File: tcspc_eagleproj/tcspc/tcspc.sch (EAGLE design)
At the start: 0 parts

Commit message: Added the THS788 to the sch, made a simple brd with the 788 on it. Created a gitattributes file so I don't keep getting crlf messages for eagle files.
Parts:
- added U1: THS788, tcspc_lib:THS788
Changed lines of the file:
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@@
 <parts>
 <part name="FRAME1" library="frames" library_urn="urn:adsk.eagle:library:229" deviceset="FRAME_A_L" device=""/>
+<part name="U1" library="tcspc_lib" deviceset="THS788" device=""/>
 </parts>
 <sheets>
@@
 <instance part="FRAME1" gate="G$1" x="0" y="0"/>
 <instance part="FRAME1" gate="G$2" x="172.72" y="0"/>
+<instance part="U1" gate="G$1" x="129.54" y="99.06"/>
 </instances>
 <busses>
+</busses>
+<nets>
+</nets>
+</sheet>
+<sheet>
+<plain>
+</plain>
+<instances>
+</instances>
+<busses>

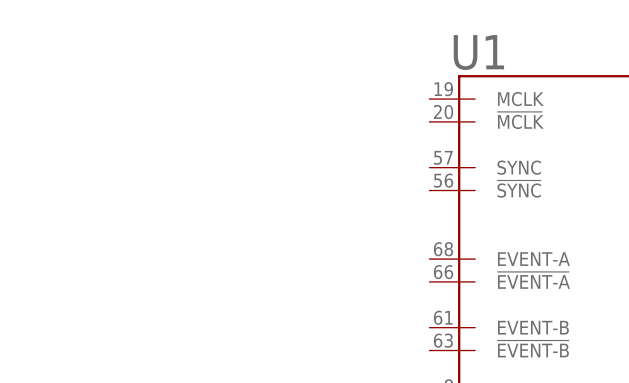
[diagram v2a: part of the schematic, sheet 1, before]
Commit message: added the SiT5021 Oscillator to the library
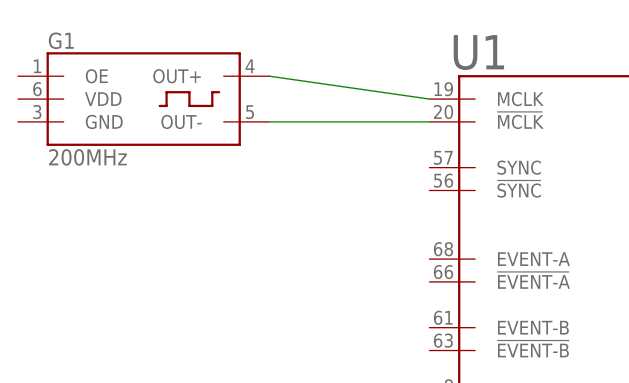
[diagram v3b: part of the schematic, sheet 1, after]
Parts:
- added G1: 200MHz, tcspc_lib:SIT5021
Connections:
- new net N$1: G1.OUT-, U1.!MCLK
- new net N$2: G1.OUT+, U1.MCLK
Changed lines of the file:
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@@
 <part name="FRAME1" library="frames" library_urn="urn:adsk.eagle:library:229" deviceset="FRAME_A_L" device=""/>
 <part name="U1" library="tcspc_lib" deviceset="THS788" device=""/>
+<part name="G1" library="tcspc_lib" deviceset="SIT5021" device="" value="200MHz"/>
 </parts>
 <sheets>
@@
 <instance part="FRAME1" gate="G$2" x="172.72" y="0"/>
 <instance part="U1" gate="G$1" x="129.54" y="99.06"/>
+<instance part="G1" gate="G$1" x="76.2" y="139.7"/>
 </instances>
 <busses>
 </busses>
 <nets>
+<net name="N$1" class="0">
+<segment>
+<pinref part="G1" gate="G$1" pin="OUT-"/>
+<pinref part="U1" gate="G$1" pin="!MCLK"/>
+<wire x1="91.44" y1="137.16" x2="109.22" y2="137.16" width="0.1524" layer="91"/>
+</segment>
+</net>
+<net name="N$2" class="0">
+<segment>
+<pinref part="U1" gate="G$1" pin="MCLK"/>
+<pinref part="G1" gate="G$1" pin="OUT+"/>
+<wire x1="109.22" y1="139.7" x2="91.44" y2="142.24" width="0.1524" layer="91"/>
+</segment>
+</net>
 </nets>
 </sheet>

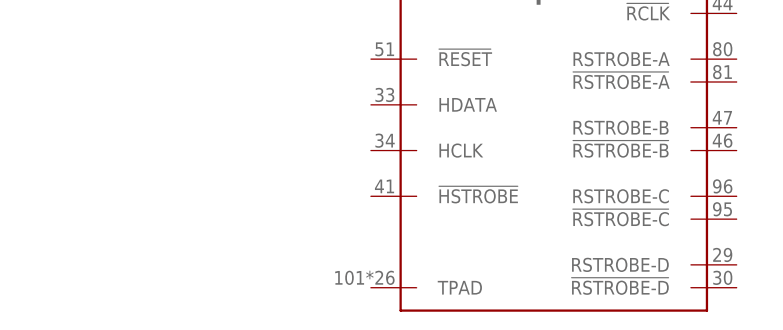
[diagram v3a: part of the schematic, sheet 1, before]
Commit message: threw a couple SMAs and DACs onto the schematic
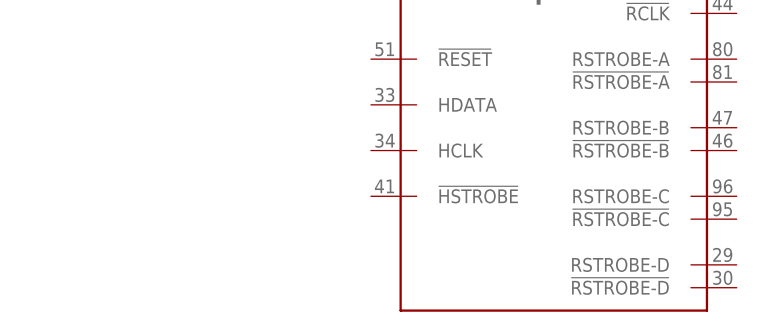
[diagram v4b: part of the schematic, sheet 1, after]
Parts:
- added U2, U3, U4, U5: MCP4725, tcspc_lib:MCP4725
- added X1, X2, X3, X4: SMA, tcspc_lib:SMA
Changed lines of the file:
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@@
 <layer number="48" name="Document" color="7" fill="1" visible="no" active="no"/>
 <layer number="49" name="Reference" color="7" fill="1" visible="no" active="no"/>
+<layer number="50" name="dxf" color="7" fill="1" visible="no" active="no"/>
 <layer number="51" name="tDocu" color="7" fill="1" visible="no" active="no"/>
 <layer number="52" name="bDocu" color="7" fill="1" visible="no" active="no"/>
+<layer number="53" name="tGND_GNDA" color="7" fill="9" visible="no" active="no"/>
+<layer number="54" name="bGND_GNDA" color="1" fill="9" visible="no" active="no"/>
+<layer number="56" name="wert" color="7" fill="1" visible="no" active="no"/>
+<layer number="57" name="tCAD" color="7" fill="1" visible="no" active="no"/>
+<layer number="59" name="tCarbon" color="7" fill="1" visible="no" active="no"/>
+<layer number="60" name="bCarbon" color="7" fill="1" visible="no" active="no"/>
 <layer number="88" name="SimResults" color="9" fill="1" visible="yes" active="yes"/>
 <layer number="89" name="SimProbes" color="9" fill="1" visible="yes" active="yes"/>
@@
 <layer number="97" name="Info" color="7" fill="1" visible="yes" active="yes"/>
 <layer number="98" name="Guide" color="6" fill="1" visible="yes" active="yes"/>
+<layer number="99" name="SpiceOrder" color="7" fill="1" visible="yes" active="yes"/>
+<layer number="100" name="Muster" color="7" fill="1" visible="no" active="no"/>
+<layer number="101" name="Patch_Top" color="12" fill="4" visible="yes" active="yes"/>
+<layer number="102" name="Vscore" color="7" fill="1" visible="yes" active="yes"/>
+<layer number="103" name="tMap" color="7" fill="1" visible="yes" active="yes"/>
+<layer number="104" name="Name" color="16" fill="1" visible="yes" active="yes"/>
+<layer number="105" name="tPlate" color="7" fill="1" visible="yes" active="yes"/>
+<layer number="106" name="bPlate" color="7" fill="1" visible="yes" active="yes"/>
+<layer number="107" name="Crop" color="7" fill="1" visible="yes" active="yes"/>
+<layer number="108" name="tplace-old" color="10" fill="1" visible="yes" active="yes"/>
+<layer number="109" name="ref-old" color="11" fill="1" visible="yes" active="yes"/>
+<layer number="110" name="fp0" color="7" fill="1" visible="yes" active="yes"/>
+<layer number="111" name="LPC17xx" color="7" fill="1" visible="yes" active="yes"/>
+<layer number="112" name="tSilk" color="7" fill="1" visible="yes" active="yes"/>
+<layer number="113" name="IDFDebug" color="7" fill="1" visible="yes" active="yes"/>
+<layer number="114" name="Badge_Outline" color="7" fill="1" visible="yes" active="yes"/>
+<layer number="115" name="ReferenceISLANDS" color="7" fill="1" visible="yes" active="yes"/>
+<layer number="116" name="Patch_BOT" color="9" fill="4" visible="yes" active="yes"/>
+<layer number="118" name="Rect_Pads" color="7" fill="1" visible="yes" active="yes"/>
+<layer number="121" name="_tsilk" color="7" fill="1" visible="yes" active="yes"/>
+<layer number="122" name="_bsilk" color="7" fill="1" visible="yes" active="yes"/>
+<layer number="123" name="tTestmark" color="7" fill="1" visible="yes" active="yes"/>
+<layer number="124" name="bTestmark" color="7" fill="1" visible="yes" active="yes"/>
+<layer number="125" name="_tNames" color="7" fill="1" visible="yes" active="yes"/>
+<layer number="126" name="_bNames" color="7" fill="1" visible="yes" active="yes"/>
+<layer number="127" name="_tValues" color="7" fill="1" visible="yes" active="yes"/>
+<layer number="128" name="_bValues" color="7" fill="1" visible="yes" active="yes"/>
+<layer number="129" name="Mask" color="7" fill="1" visible="yes" active="yes"/>
+<layer number="131" name="tAdjust" color="7" fill="1" visible="yes" active="yes"/>
+<layer number="132" name="bAdjust" color="7" fill="1" visible="yes" active="yes"/>
+<layer number="144" name="Drill_legend" color="7" fill="1" visible="yes" active="yes"/>
+<layer number="150" name="Notes" color="7" fill="1" visible="yes" active="yes"/>
+<layer number="151" name="HeatSink" color="7" fill="1" visible="yes" active="yes"/>
+<layer number="152" name="_bDocu" color="7" fill="1" visible="yes" active="yes"/>
+<layer number="153" name="FabDoc1" color="7" fill="1" visible="yes" active="yes"/>
+<layer number="154" name="FabDoc2" color="7" fill="1" visible="yes" active="yes"/>
+<layer number="155" name="FabDoc3" color="7" fill="1" visible="yes" active="yes"/>
+<layer number="199" name="Contour" color="7" fill="1" visible="yes" active="yes"/>
+<layer number="200" name="200bmp" color="1" fill="10" visible="yes" active="yes"/>
+<layer number="201" name="201bmp" color="2" fill="10" visible="yes" active="yes"/>
+<layer number="202" name="202bmp" color="3" fill="10" visible="yes" active="yes"/>
+<layer number="203" name="203bmp" color="4" fill="10" visible="yes" active="yes"/>
+<layer number="204" name="204bmp" color="5" fill="10" visible="yes" active="yes"/>
+<layer number="205" name="205bmp" color="6" fill="10" visible="yes" active="yes"/>
+<layer number="206" name="206bmp" color="7" fill="10" visible="yes" active="yes"/>
+<layer number="207" name="207bmp" color="8" fill="10" visible="yes" active="yes"/>
+<layer number="208" name="208bmp" color="9" fill="10" visible="yes" active="yes"/>
+<layer number="209" name="209bmp" color="7" fill="1" visible="yes" active="yes"/>
+<layer number="210" name="210bmp" color="7" fill="1" visible="yes" active="yes"/>
+<layer number="211" name="211bmp" color="7" fill="1" visible="yes" active="yes"/>
+<layer number="212" name="212bmp" color="7" fill="1" visible="yes" active="yes"/>
+<layer number="213" name="213bmp" color="7" fill="1" visible="yes" active="yes"/>
+<layer number="214" name="214bmp" color="7" fill="1" visible="yes" active="yes"/>
+<layer number="215" name="215bmp" color="7" fill="1" visible="yes" active="yes"/>
+<layer number="216" name="216bmp" color="7" fill="1" visible="yes" active="yes"/>
+<layer number="217" name="217bmp" color="18" fill="1" visible="no" active="no"/>
+<layer number="218" name="218bmp" color="19" fill="1" visible="no" active="no"/>
+<layer number="219" name="219bmp" color="20" fill="1" visible="no" active="no"/>
+<layer number="220" name="220bmp" color="21" fill="1" visible="no" active="no"/>
+<layer number="221" name="221bmp" color="22" fill="1" visible="no" active="no"/>
+<layer number="222" name="222bmp" color="23" fill="1" visible="no" active="no"/>
+<layer number="223" name="223bmp" color="24" fill="1" visible="no" active="no"/>
+<layer number="224" name="224bmp" color="25" fill="1" visible="no" active="no"/>
+<layer number="225" name="225bmp" color="7" fill="1" visible="yes" active="yes"/>
+<layer number="226" name="226bmp" color="7" fill="1" visible="yes" active="yes"/>
+<layer number="227" name="227bmp" color="7" fill="1" visible="yes" active="yes"/>
+<layer number="228" name="228bmp" color="7" fill="1" visible="yes" active="yes"/>
+<layer number="229" name="229bmp" color="7" fill="1" visible="yes" active="yes"/>
+<layer number="230" name="230bmp" color="7" fill="1" visible="yes" active="yes"/>
+<layer number="231" name="231bmp" color="7" fill="1" visible="yes" active="yes"/>
+<layer number="232" name="Eagle3D_PG2" color="7" fill="1" visible="yes" active="yes"/>
+<layer number="233" name="Eagle3D_PG3" color="7" fill="1" visible="yes" active="yes"/>
+<layer number="248" name="Housing" color="7" fill="1" visible="yes" active="yes"/>
+<layer number="249" name="Edge" color="7" fill="1" visible="yes" active="yes"/>
+<layer number="250" name="Descript" color="3" fill="1" visible="no" active="no"/>
+<layer number="251" name="SMDround" color="12" fill="11" visible="no" active="no"/>
+<layer number="254" name="cooling" color="7" fill="1" visible="yes" active="yes"/>
+<layer number="255" name="routoute" color="7" fill="1" visible="yes" active="yes"/>
 </layers>
 <schematic xreflabel="%F%N/%S.%C%R" xrefpart="/%S.%C%R">
@@
 <part name="U1" library="tcspc_lib" deviceset="THS788" device=""/>
 <part name="G1" library="tcspc_lib" deviceset="SIT5021" device="" value="200MHz"/>
+<part name="FRAME2" library="frames" library_urn="urn:adsk.eagle:library:229" deviceset="FRAME_A_L" device=""/>
+<part name="X1" library="tcspc_lib" deviceset="SMA" device=""/>
+<part name="X2" library="tcspc_lib" deviceset="SMA" device=""/>
+<part name="X3" library="tcspc_lib" deviceset="SMA" device=""/>
+<part name="X4" library="tcspc_lib" deviceset="SMA" device=""/>
+<part name="U2" library="tcspc_lib" deviceset="MCP4725" device=""/>
+<part name="U3" library="tcspc_lib" deviceset="MCP4725" device=""/>
+<part name="U4" library="tcspc_lib" deviceset="MCP4725" device=""/>
+<part name="U5" library="tcspc_lib" deviceset="MCP4725" device=""/>
 </parts>
 <sheets>
@@
 </plain>
 <instances>
+<instance part="FRAME2" gate="G$1" x="0" y="0"/>
+<instance part="FRAME2" gate="G$2" x="172.72" y="0"/>
+<instance part="X1" gate="G$1" x="38.1" y="187.96"/>
+<instance part="X2" gate="G$1" x="38.1" y="175.26"/>
+<instance part="X3" gate="G$1" x="38.1" y="162.56"/>
+<instance part="X4" gate="G$1" x="38.1" y="149.86"/>
+<instance part="U2" gate="G$1" x="96.52" y="193.04"/>
+<instance part="U3" gate="G$1" x="96.52" y="167.64"/>
+<instance part="U4" gate="G$1" x="96.52" y="142.24"/>
+<instance part="U5" gate="G$1" x="96.52" y="116.84"/>
 </instances>
 <busses>
